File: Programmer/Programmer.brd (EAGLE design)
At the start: 49.5 x 55.9 mm, 33 parts, among them Q2 16Mhz, U1 ATTINY84, X2 C-GRID-04-70543, X3 C-GRID-04-70543

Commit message: various minor changes
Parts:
- moved LED1 6.35 mm to (43.5, 54.3)
- moved R1 6.35 mm to (47.0, 54.3)
- moved D3 6.35 mm to (16.8, 46.4)
- moved R2 6.35 mm to (20.3, 46.4)
- moved R4 6.35 mm to (20.3, 48.3)
- moved ICSP 6.35 mm to (33.0, 30.5)
- moved U$1 6.35 mm to (31.6, 22.9)
- moved U$5 6.35 mm to (44.8, 25.4)
- moved JP10 6.35 mm to (41.9, 48.3)
- moved JP11 6.35 mm to (13.8, 21.6)
- moved U$4 6.35 mm to (8.26, 25.4)
- moved X3 6.35 mm to (19.1, 29.5)
- moved C1 6.35 mm to (25.7, 44.5)
- moved F1 6.35 mm to (25.7, 53.3)
- moved JP1 6.35 mm to (25.7, 53.3)
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
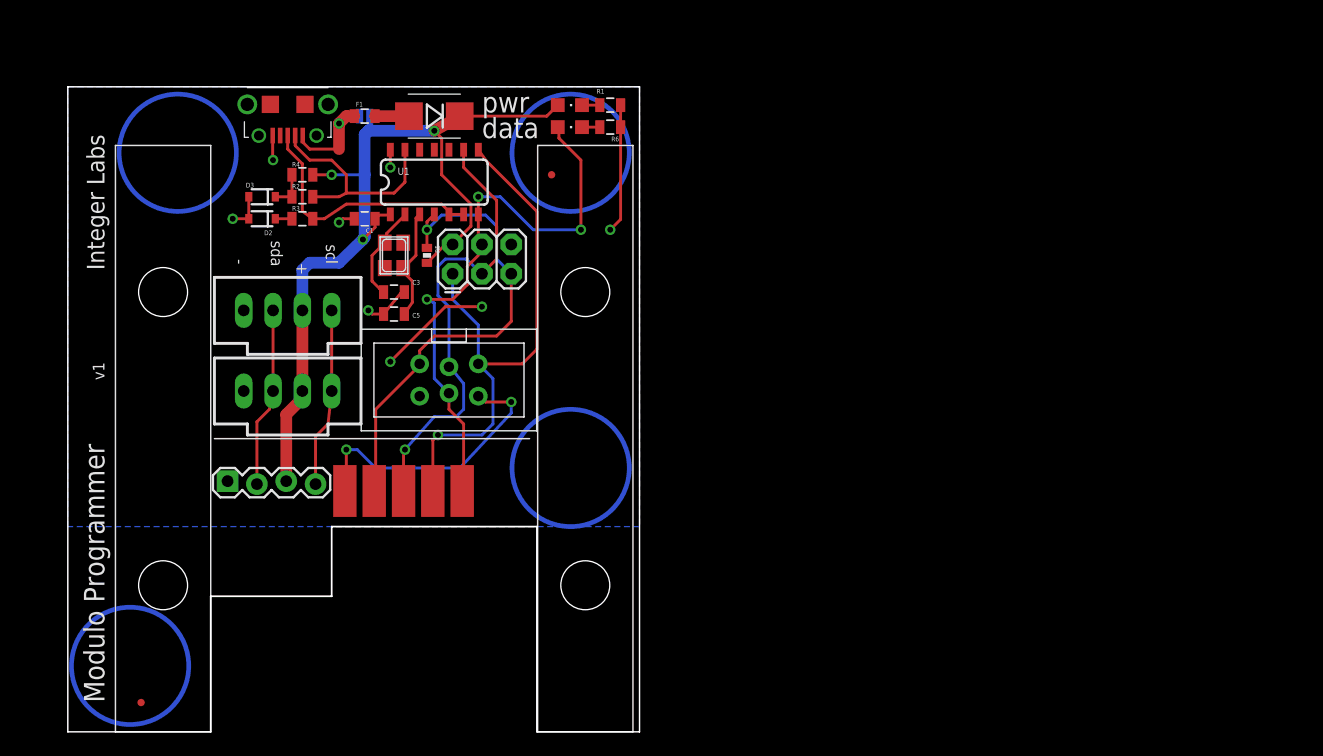
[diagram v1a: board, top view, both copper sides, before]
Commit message: Major revision of all boards. Cleaned up old files. Exported BOM csv files for all boards
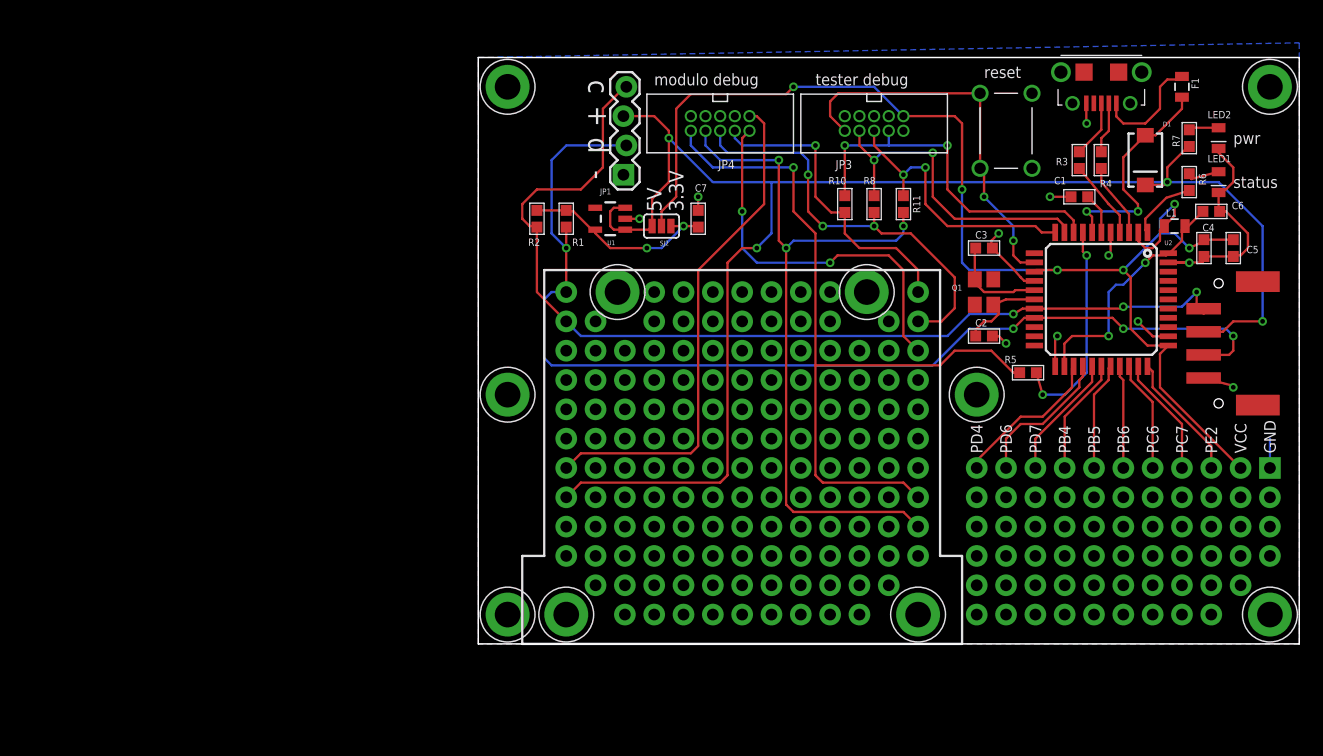
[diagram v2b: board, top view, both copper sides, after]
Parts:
- removed D2, D3: 3.6V, SparkFun-DiscreteSemi:SOD-323
- removed ICSP: AVRISP-BOX, adafruit:AVRISP-BOX
- removed Q2: 16Mhz, adafruit:NX3225
- removed U$15: USBFCI-MICROB, IntegerLabs:USB-MICROB-FCI
- removed U$22, U$23, U$24: SPRING-CONNECTOR, IntegerLabs:SPRING-CONNECTOR
- removed X2, X3: C-GRID-04-70543, con-molex:70543-04
- added C2: 18pF, Modulo:0603
- added C4, C6, C7: .1uF, Modulo:0603
- added JP12, JP13, JP14, JP15, JP16, JP17, JP2, JP24, JP25, JP34, JP35, JP5, JP6, JP7: M10NO_SILK, SparkFun-Connectors:1X10_NO_SILK
- added JP18, JP19: (no value), SparkFun-Connectors:1X05_NO_SILK
- added JP20, JP21, JP22, JP23: M01SMDNS, SparkFun-Connectors:1X01NS
- added JP26, JP27, JP28: (no value), SparkFun-Connectors:1X03_NO_SILK
- added JP3, JP4: ICSP, Modulo:2X5-.05
- added JP33: (no value), SparkFun-Connectors:1X04_NO_SILK
- added L1: (no value), IntegerLabs:0805
- added Q1: 16Mhz, Modulo:NX3225
- added R10, R11, R8: 4.7k, Modulo:0603
- added R7: 681Ω, Modulo:0603
- added SJ2: (no value), SparkFun-Passives:SJ_3_PASTE1&2
- added SW1: SWITCHMJTP1234, Modulo:MJTP1234
- added U$10, U$11, U$3, U$6, U$8, U$9: HOLE#2, Modulo:HOLE-#2
- added U$7: JST-PA-TOP-SMD, Modulo:JST-PA-TOP-SMD
- added U2: ATMEGA32U4TQFP, SparkFun-DigitalIC:SPARKFUN-DIGITALIC_TQFP44
- added U3: USBFCI-MICROB, IntegerLabs:USB-MICROB-FCI
- C1: value 0.47uF -> 1uF; device SparkFun-Capacitors:0805 -> Modulo:0603
- C3: device SparkFun-Capacitors:0805 -> Modulo:0603
- C5: value 18pF -> 10uF; device SparkFun-Capacitors:0805 -> Modulo:0603
- D1: value (none) -> DIODE-SCHOTTKY_; device SparkFun-DiscreteSemi:SMB-DIODE -> SparkFun-DiscreteSemi:SMA-DIODE
- F1: value (none) -> MF-PSMF110X-2; device SparkFun-Passives:0805 -> Modulo:0805
- JP1: device SparkFun-Passives:SJ_2S-NO -> SparkFun-Connectors:1X04_LOCK
- JP10, JP8: value FIDUCIALUFIDUCIAL -> M10NO_SILK; device SparkFun:MICRO-FIDUCIAL -> SparkFun-Connectors:1X10_NO_SILK
- JP11: value (none) -> M10NO_SILK; device SparkFun-Connectors:1X04_LOCK -> SparkFun-Connectors:1X10_NO_SILK
- JP9: value (none) -> M10NO_SILK; device SparkFun-Connectors:2X3 -> SparkFun-Connectors:1X10_NO_SILK
- LED1, LED2: value (none) -> blue; device adafruit:CHIPLED_0805 -> Modulo:0805-LED
- R1: value 680 -> 1.5KΩ; device SparkFun-Passives:0805 -> Modulo:0603
- R2: value 68 -> 1.5KΩ; device SparkFun-Resistors:0805 -> Modulo:0603
- R3: value 68 -> 22Ω; device SparkFun-Resistors:0805 -> Modulo:0603
- R4: value 1.5K -> 22Ω; device SparkFun-Resistors:0805 -> Modulo:0603
- R5: value 10k -> 4.7k; device SparkFun-Passives:0402-RES -> Modulo:0603
- R6: value 680 -> 681Ω; device SparkFun-Passives:0805 -> Modulo:0603
- U$1, U$2: value SPRING-CONNECTOR -> HOLE#2; device IntegerLabs:SPRING-CONNECTOR -> Modulo:HOLE-#2
- U$4, U$5: value (none) -> HOLE#2; device IntegerLabs:CARD-GUIDE-2" -> Modulo:HOLE-#2
- U1: value ATTINY84 -> MIC5205-3.3YM5 TR; device SparkFun-DigitalIC:SO14 -> Modulo:SOT23-5
- moved C5 72.9 mm to (101.0, 41.9), turned to 270 degrees
- moved F1 70.8 mm to (96.5, 55.9), turned to 270 degrees
- moved R4 69.2 mm to (89.5, 49.5), turned to 270 degrees
- moved R3 67.5 mm to (87.6, 49.5), turned to 270 degrees
- moved U$4 62.3 mm to (69.2, 38.1)
- moved C1 61.9 mm to (87.6, 46.4)
- moved D1 61.7 mm to (93.3, 49.5), turned to 270 degrees
- moved LED1 56.6 mm to (99.7, 47.6), turned to 180 degrees
- moved LED2 56.2 mm to (99.7, 51.4), turned to 180 degrees
- moved R5 53.1 mm to (83.2, 31.1), turned to 0 degrees
- moved C3 51.3 mm to (79.4, 41.9)
- moved R6 50.4 mm to (97.2, 47.6), turned to 90 degrees
- moved U$2 48.8 mm to (73.7, 10.2), turned to 0 degrees
- moved JP10 46.0 mm to (71.1, 12.7), turned to 90 degrees
- moved JP9 46.0 mm to (68.6, 10.2), turned to 90 degrees
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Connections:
- removed net G1: Q2.4
- removed net G2: Q2.2
- removed net N$3: C5.1, Q2.1, U1.3
- removed net RST: U1.10
- removed net VPROG: ICSP.2, U$24.P$1
- new net +3.3V: C7.1, R1.1, R2.1, SJ2.1, U1.5
- new net +5V: D1.C, JP1.3, JP34.8, R7.1, SJ2.3, U$7.3, U1.1, U1.3
- new net DUT_MISO: JP35.2, JP4.6, R8.1
- new net DUT_MOSI: JP35.9, JP4.8, R11.1
- new net DUT_RESET: JP35.8, JP4.10, R5.1
- new net DUT_RESET_5V: R5.2, U2.8
- new net DUT_SCK: JP35.1, JP4.4, R10.1
- new net DUT_SWDIO: JP35.3, JP4.2
- new net DUT_VPROG: JP34.7, JP4.1
- new net LED: R6.1, U2.1
- new net N$11: U2.36
- new net N$12: LED2.A, R7.2
- new net N$15: C2.1, Q1.1, U2.17
- new net N$4: C3.1, Q1.3, U2.16
- new net N$8: R3.2, U2.4
- new net PB4: JP2.4, U2.28
- new net PB5: JP2.5, U2.29
- new net PB6: JP2.6, U2.30
- new net PC6: JP2.7, U2.31
- new net PC7: JP2.8, U2.32
- new net PD4: JP2.1, U2.25
- new net PD6: JP2.2, U2.26
- new net PD7: JP2.3, U2.27
- new net PE2: JP2.9, U2.33
- new net VBUS: D1.A, F1.2, U2.7
- new net VIN: F1.1, U3.P1
- net D+: now also R3.1, U3.P3; no longer R3.2, U$15.P3, U1.5, U1.6
- net D-: now also R4.1, U3.P2; no longer R2.2, U$15.P2, U1.13
- net GND: now also C2.2, C4.2, C6.2, C7.2, JP1.1, JP3.3, JP3.5, JP3.9, JP33.1, JP34.9, JP4.3, JP4.5, JP4.9, LED1.C, LED2.C, SW1.P$1, SW1.P$2, U$7.1, U1.2, U2.15, U2.23, U2.35, U2.43, U2.5, U3.P5; no longer D2.2, D3.2, ICSP.6, JP11.1, JP9.6, R1.1, R6.1, U$15.P5, U1.14, X2.1, X3.1
- net MISO: now also JP3.6, R11.2, U2.11; no longer ICSP.1, JP9.1, U$1.P$1, U1.8
- net MOSI: now also JP3.8, R8.2, U2.10; no longer ICSP.4, JP9.4, LED2.A, U$23.P$1, U1.7
- net N$1: now also C1.1, U2.6; no longer D1.A, F1.2
- net N$10: now also U2.37; no longer C3.1, Q2.3, U1.2
- net N$2: now also C6.1, L1.2, U2.24, U2.44; no longer LED2.C, R6.2
- net N$5: now also LED1.A, R6.2; no longer F1.1, JP1.2, U$15.P1
- net N$6: now also U2.39; no longer D3.1, R2.1, R4.1
- net N$7: now also U2.38; no longer D2.1, R3.1
- net N$9: now also R4.2, U2.3; no longer LED1.C, R1.2
- net RESET: now also JP3.10, SW1.P$3, SW1.P$4, U2.13; no longer ICSP.5, JP9.5, R5.1, U$2.P$1, U1.4
- net SCK: now also JP3.4, R10.2, U2.9; no longer ICSP.3, JP9.3, U$22.P$1, U1.9
- net SCL: now also JP1.4, JP34.2, R2.2, U$7.4, U2.18; no longer JP11.4, X2.4, X3.4
- net SDA: now also JP1.2, JP34.1, R1.2, U$7.2, U2.19; no longer JP11.2, X2.2, X3.2
- net VCC: now also C4.1, C5.1, JP2.10, JP3.1, L1.1, SJ2.2, U2.14, U2.2, U2.34; no longer C1.1, D1.C, JP1.1, JP11.3, JP9.2, LED1.A, R4.2, R5.2, U1.1, X2.3, X3.3
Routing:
- net +5V: track 0.00 -> 136.7 mm, vias 0 -> 4
- net SDA: track 15.5 -> 94.3 mm, vias 0 -> 4
- net SCL: track 15.5 -> 87.5 mm, vias 0 -> 3
- net DUT_RESET: track 0.00 -> 67.1 mm, vias 0 -> 1
- net DUT_MOSI: track 0.00 -> 63.0 mm, vias 0 -> 3
- net DUT_VPROG: track 0.00 -> 44.1 mm
- net DUT_MISO: track 0.00 -> 36.4 mm, vias 0 -> 3
- net VCC: track 76.1 -> 110.4 mm, vias 3 -> 6
- net DUT_SWDIO: track 0.00 -> 33.2 mm, vias 0 -> 2
- net DUT_SCK: track 0.00 -> 26.8 mm, vias 0 -> 1
- net VPROG: track 25.7 -> 0.00 mm, vias 2 -> 0
- net MISO: track 49.6 -> 24.3 mm, vias 1 -> 2
- net MOSI: track 50.1 -> 28.3 mm, vias 3 -> 2
- net N$2: track 1.54 -> 21.5 mm, vias 0 -> 2
- net VBUS: track 0.00 -> 19.5 mm, vias 0 -> 2
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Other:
- board size 49.5 x 55.9 mm -> 71.1 x 50.8 mm
- board text added: "3.3V"
- board text added: "5V"
- board text added: "GND"
- board text added: "PB4"
- board text added: "PB5"
- board text added: "PB6"
- board text added: "PC6"
- board text added: "PC7"
- board text added: "PD4"
- board text added: "PD6"
- board text added: "PD7"
- board text added: "PE2"
- board text added: "VCC"
- board text added: "c"
- board text added: "d"
- board text added: "modulo debug"
- board text added: "reset"
- board text added: "status"
- board text added: "tester debug"
- board text removed: "Integer Labs"
- board text removed: "Modulo Programmer"
- board text removed: "data"
- board text removed: "scl"
- board text removed: "sda"
- board text removed: "v1"

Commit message: Check point of current PCB designs. Among other things I think this change includes rewiring of programming lines on many of the boards,.
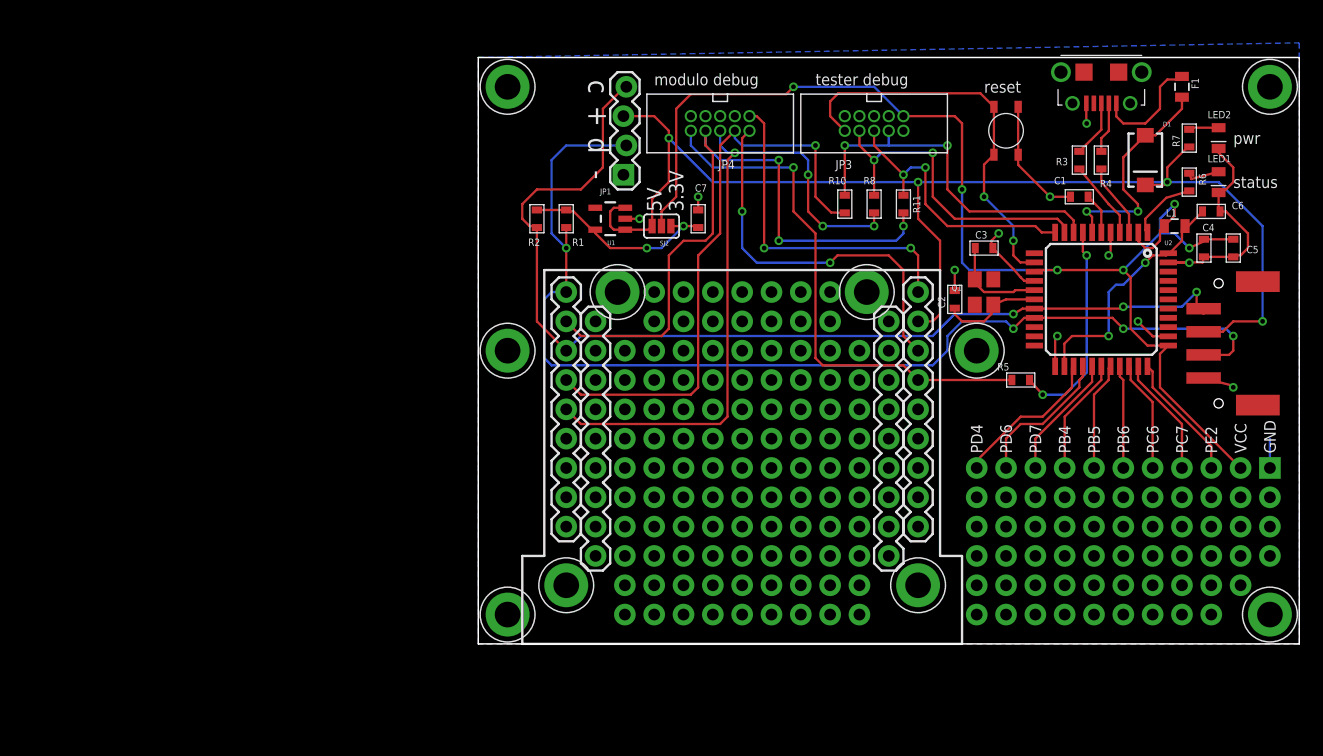
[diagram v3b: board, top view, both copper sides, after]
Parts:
- JP10, JP34, JP35, JP7: value M10NO_SILK -> M09; device SparkFun-Connectors:1X10_NO_SILK -> SparkFun-Connectors:1X09
- R10, R11, R5, R8: value 4.7k -> 1.5KΩ
- SW1: value SWITCHMJTP1234 -> SWITCH-PTS-810; device Modulo:MJTP1234 -> Modulo:TACT-SWITCH-PTS-810
- moved C2 4.07 mm to (76.8, 37.5), turned to 90 degrees
- moved U$5 3.81 mm to (38.1, 33.0)
- moved U$6 3.81 mm to (78.7, 33.0)
- moved JP10 2.54 mm to (71.1, 15.2)
- moved JP7 2.54 mm to (45.7, 15.2)
- moved U$1 2.54 mm to (43.2, 12.7)
- moved U$2 2.54 mm to (73.7, 12.7)
- moved R5 0.90 mm to (82.5, 30.5)
- turned SW1 to 90 degrees
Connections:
- net +5V: now also JP35.2; no longer JP34.8
- net DUT_MISO: now also JP34.5; no longer JP35.2
- net DUT_MOSI: now also JP34.2; no longer JP35.9
- net DUT_RESET: now also JP35.4; no longer JP35.8
- net DUT_SCK: now also JP34.4; no longer JP35.1
- net DUT_VPROG: now also JP35.1; no longer JP34.7
- net GND: now also JP35.5, SW1.P$3, SW1.P$4; no longer JP34.9, SW1.P$1, SW1.P$2
- net RESET: now also SW1.P$1, SW1.P$2; no longer SW1.P$3, SW1.P$4
- net SCL: now also JP34.3; no longer JP34.2
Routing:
- net +5V: track 136.7 -> 108.6 mm
- net DUT_SCK: track 26.8 -> 51.2 mm
- net DUT_MISO: track 36.4 -> 59.1 mm, vias 3 -> 4
- net DUT_RESET: track 67.1 -> 46.2 mm
- net DUT_VPROG: track 44.1 -> 29.1 mm, vias 0 -> 2
- net GND: track 47.8 -> 57.0 mm
- net DUT_MOSI: track 63.0 -> 57.7 mm
- net SCL: track 87.5 -> 90.0 mm
- net N$15: track 7.76 -> 9.40 mm
- net SDA: track 94.3 -> 95.6 mm
- net RESET: track 33.7 -> 34.4 mm
